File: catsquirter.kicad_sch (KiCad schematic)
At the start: 11 parts, among them J1 Pump, J2 Batt, J3 Batt Out, Q1 LL014N, U1 WeMos_mini

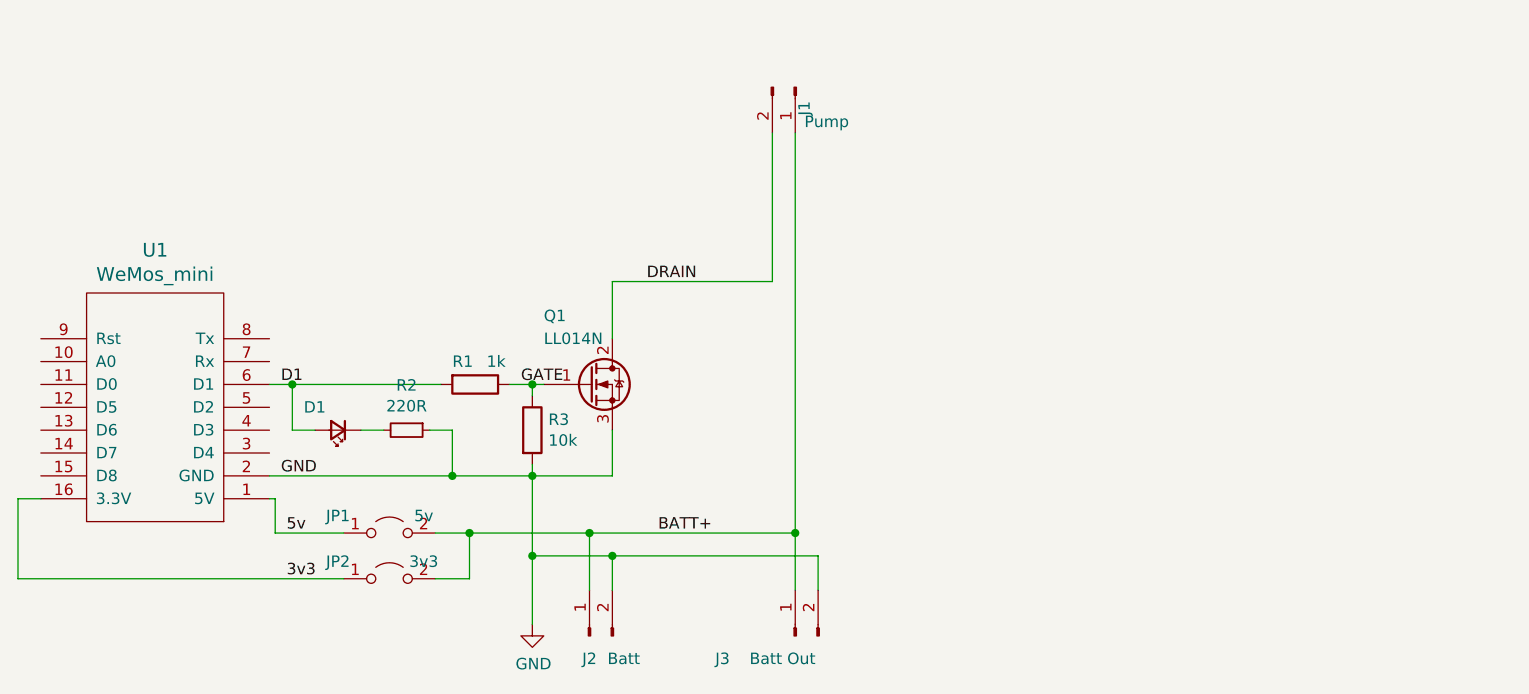
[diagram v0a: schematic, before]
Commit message: Add pin/volt jumpers. Rename project files d1_mosfet_hat -> catsquirter.
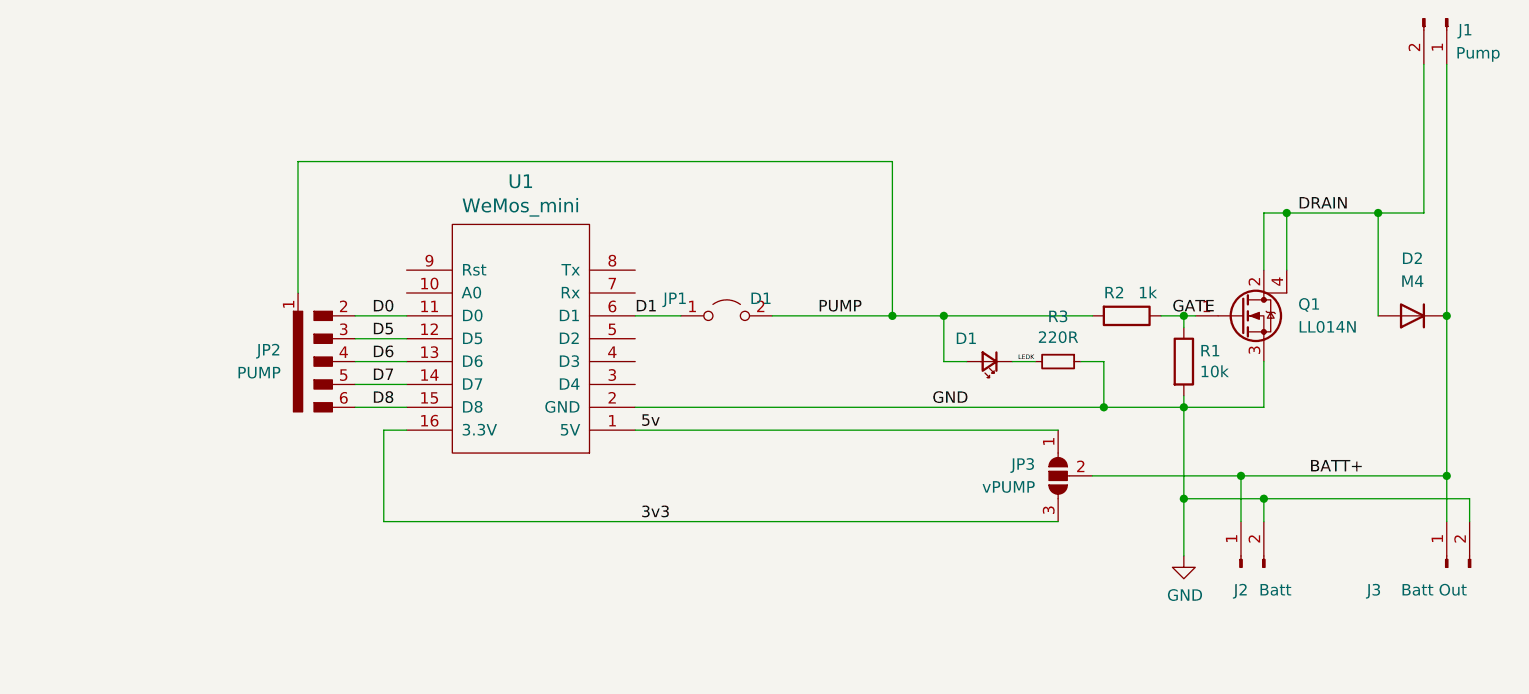
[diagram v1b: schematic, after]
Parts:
- removed JP2: 3v3, Jumper:SolderJumper-2_P1.3mm_Open_RoundedPad1.0x1.5mm, symbol Jumper:Jumper_2_Open
- removed Q1: LL014N, TO_SOT_Packages_SMD:SOT-223, symbol d1_mosfet_hat-rescue:Q_NMOS_GDS-device
- added D2: M4, Diode_SMD:D_SMB, symbol Device:D
- added JP2: PUMP, Accelerando:SolderJumper-5_P1.3mm_Open_Pad1.0x1.5mm, symbol Accelerando:SolderJumper_SP5T_Open
- added JP3: vPUMP, Jumper:SolderJumper-3_P2.0mm_Open_TrianglePad1.0x1.5mm, symbol Jumper:SolderJumper_3_Open
- added Q1: LL014N, Package_TO_SOT_SMD:SOT-223, symbol Device:Q_NMOS_GDSD
- JP1: value 5v -> D1
- renumbered R3 to R1, R1 to R2, R2 to R3
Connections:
- net 3v3: now also JP3.3 (B)
- net 5v: now also JP3.1 (A); no longer JP1.1 (A)
- net BATT+: now also D2.1 (K), JP3.2 (C); no longer JP1.2 (B)
- net D1: now also JP1.1 (A); no longer D1.2 (A), R2.2
- net DRAIN: now also D2.2 (A), Q1.2 (D), Q1.4 (D)
- net GATE: now also Q1.1 (G)
- net GND: now also Q1.3 (S)
- net D0: now reaches U1.11 (D0)
- net D0: now also JP2.2 (A)
- net D5: now reaches U1.12 (D5)
- net D5: now also JP2.3 (B)
- net D6: now reaches U1.13 (D6)
- net D6: now also JP2.4 (C)
- net D7: now reaches U1.14 (D7)
- net D7: now also JP2.5 (D)
- net D8: now reaches U1.15 (D8)
- net D8: now also JP2.6 (E)
- net LEDK: now reaches D1.1 (K), R3.2
- new net PUMP: D1.2 (A), JP1.2 (B), JP2.1 (A), R2.2
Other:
- moved on the sheet: D1, J1, J2, J3, R1, R2, R3, U1
